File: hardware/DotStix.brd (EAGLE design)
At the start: 20.3 x 50 mm, 20 parts, among them U1 ATMEGA328P-MU-QFN32

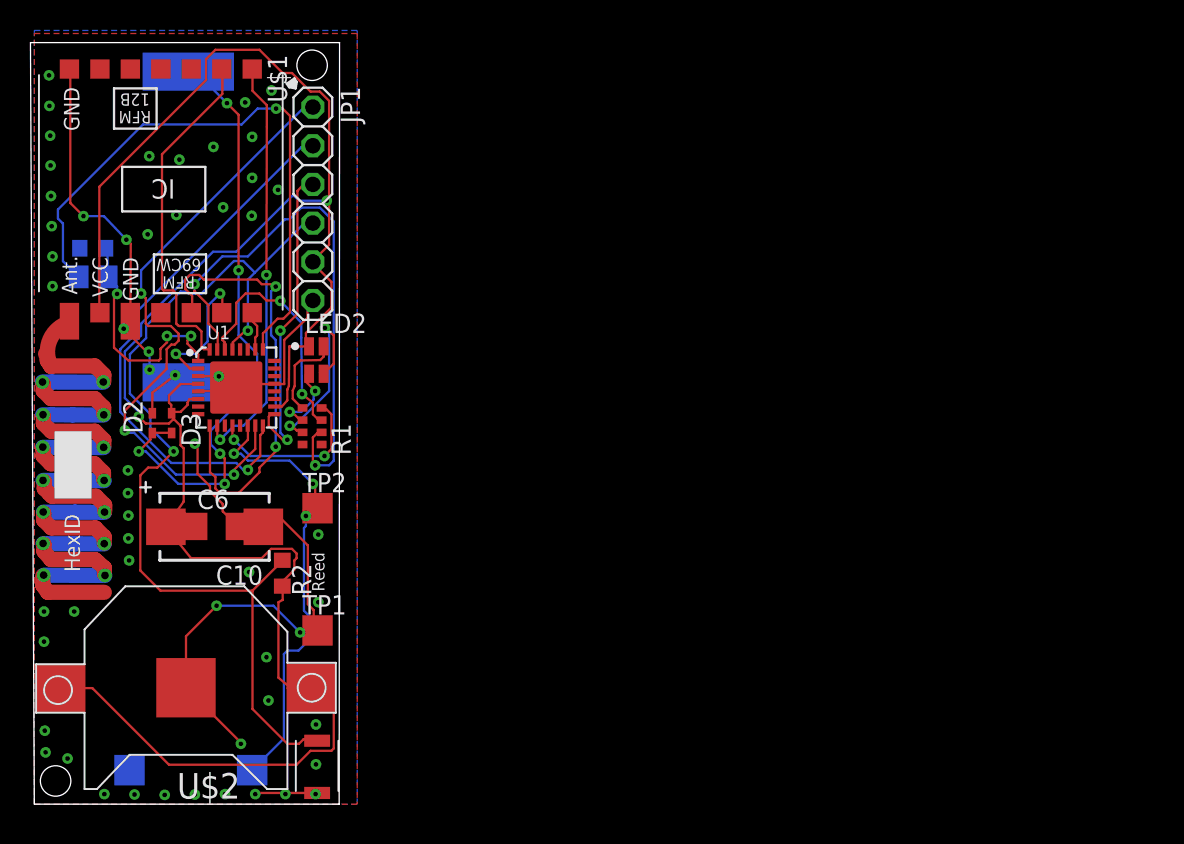
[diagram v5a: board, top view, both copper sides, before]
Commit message: Draft: Fix solar polarity, add 20ppm crystal
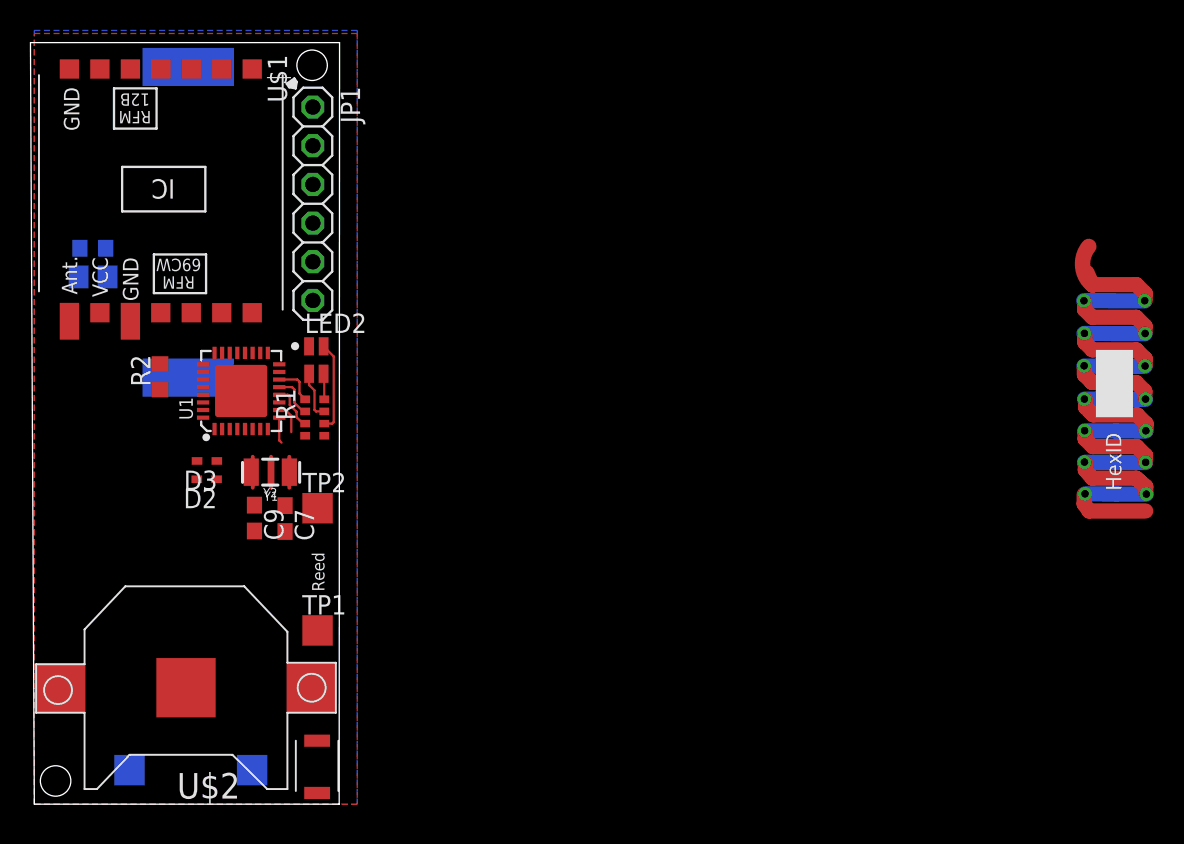
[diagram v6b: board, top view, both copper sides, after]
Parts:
- removed C10: 1500uF 4V, adafruit:CT7343
- removed C6: 100uF 4V, adafruit:C3216
- added C7, C9: 7pF, rcl:C0603
- added Y1: (no value), SparkFun-Clocks:RESONATOR-SMD-3.2X1.3
- added Y2: (no value), SparkFun-Clocks:CRYSTAL-SMD-3.2X1.5MM
- moved R2 15.2 mm to (8.25, 28.1), turned to 90 degrees
- moved D2 5.13 mm to (11.4, 21.3), turned to 180 degrees
- moved D3 3.47 mm to (11.4, 22.5), turned to 180 degrees
- moved R1 0.60 mm to (18.4, 25.4), turned to 270 degrees
- moved U1 0.39 mm to (13.6, 27.1), turned to 90 degrees
- moved D1 0.31 mm to (10.1, 38.2), turned to 270 degrees
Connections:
- removed net ADCENA: U1.13
- removed net LED: R1.4, U1.12
- removed net N$12: LED2.2, R1.6
- removed net N$5: LED2.3, R1.7
- removed net N$9: LED2.1, R1.5
- removed net RXD: R1.3, U1.30
- removed net TXD: R1.2, U1.31
- new net LED_BLUE: R1.2, U1.13
- new net LED_GREEN: R1.1, U1.14
- new net LED_RED: R1.3, U1.12
- new net N$1: LED2.2, R1.7
- new net N$3: LED2.3, R1.8
- new net N$4: LED2.1, R1.6
- new net XTAL1: C9.1, U1.7, Y1.3, Y2.P$2
- new net XTAL2: C7.1, U1.8, Y1.1, Y2.P$1
- net +3V3: no longer C10.+, C6.1
- net GND: now also C7.2, C9.2, D1.-, Y1.2; no longer C10.-, C6.2, D1.+
- net REED: now also U1.31; no longer U1.14
- net SOLAR_RAW: now also D1.+; no longer D1.-
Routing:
- net +3V3: track 142.1 -> 0.00 mm, vias 2 -> 0
- net GND: track 89.2 -> 0.00 mm, vias 57 -> 0
- net RST: track 63.1 -> 0.00 mm, vias 2 -> 0
- net MOSI: track 41.9 -> 0.00 mm, vias 3 -> 0
- net SOLAR_RAW: track 40.4 -> 0.00 mm, vias 5 -> 0
- net LIGHT_SENSE_ENA: track 39.5 -> 0.00 mm, vias 1 -> 0
- net MISO: track 36.5 -> 0.00 mm, vias 1 -> 0
- net TXD: track 36.2 -> 0.00 mm, vias 2 -> 0
- net REED: track 32.0 -> 0.00 mm, vias 3 -> 0
- net RSDI: track 29.5 -> 1.70 mm, vias 2 -> 0
- net RSDO: track 27.4 -> 2.02 mm, vias 2 -> 0
- net RIRQ: track 22.7 -> 0.00 mm
- net SCK: track 20.8 -> 0.00 mm, vias 2 -> 0
- net RXD: track 15.9 -> 0.00 mm, vias 2 -> 0
- net LIGHT_SENSE: track 15.7 -> 0.00 mm, vias 3 -> 0
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
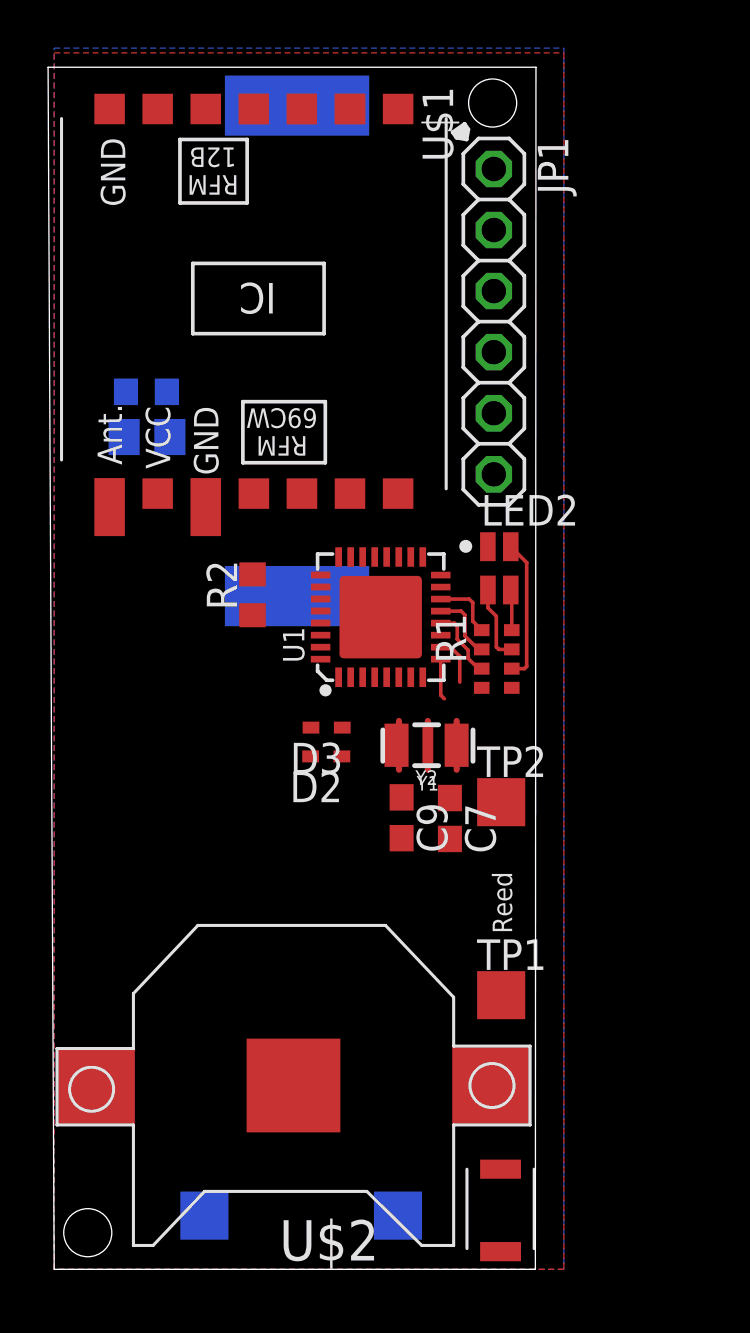
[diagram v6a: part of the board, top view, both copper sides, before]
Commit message: Draft: Fix solar polarity, add 20ppm crystal
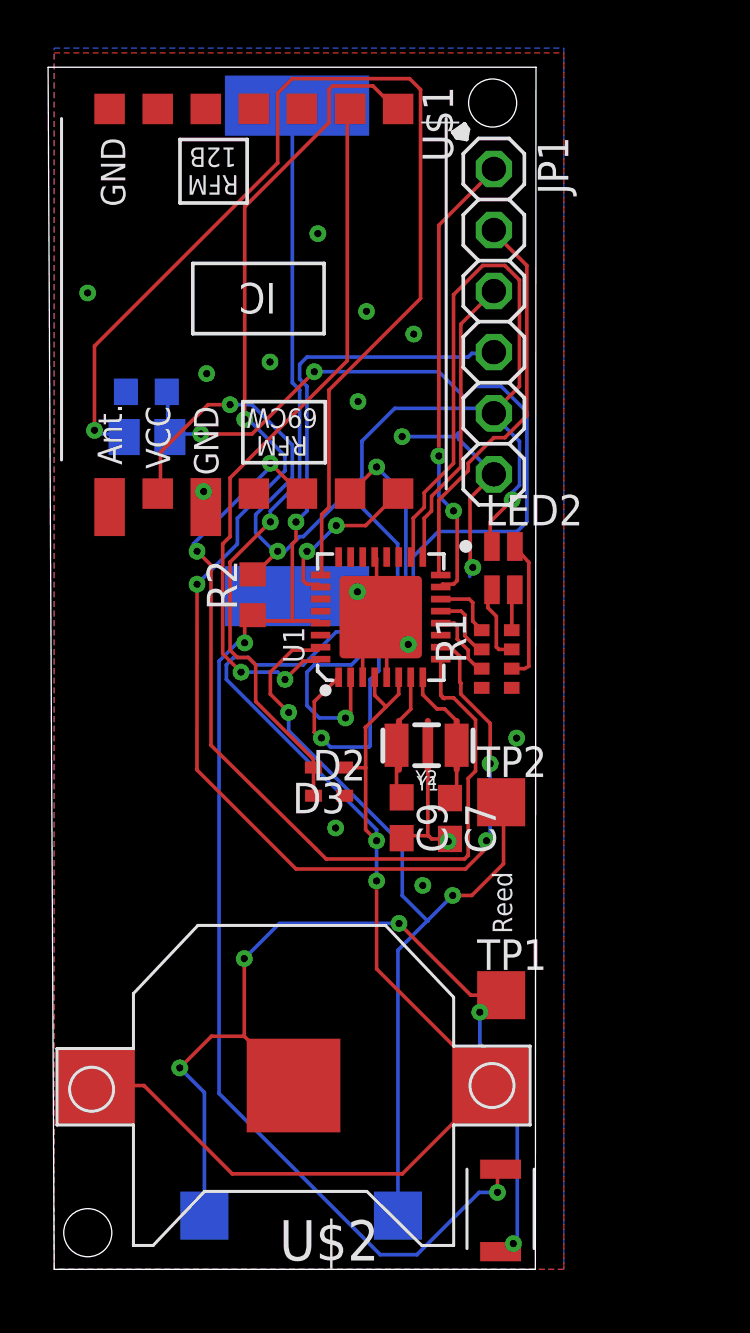
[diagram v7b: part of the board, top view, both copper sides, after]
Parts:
- moved D3 1.66 mm to (11.5, 20.9)
- moved D2 1.64 mm to (11.4, 19.7), turned to 0 degrees
- moved LED2 0.17 mm to (18.7, 29.2)
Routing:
- net +3V3: track 0.00 -> 121.2 mm, vias 0 -> 5
- net GND: track 0.00 -> 70.2 mm, vias 0 -> 21
- net RST: track 0.00 -> 59.4 mm, vias 0 -> 3
- net RSDO: track 2.02 -> 59.0 mm, vias 0 -> 4
- net LIGHT_SENSE_ENA: track 0.00 -> 46.9 mm, vias 0 -> 1
- net LIGHT_SENSE: track 0.00 -> 42.9 mm, vias 0 -> 3
- net RSDI: track 1.70 -> 37.2 mm, vias 0 -> 2
- net REED: track 0.00 -> 35.1 mm, vias 0 -> 2
- net SOLAR_RAW: track 0.00 -> 31.8 mm, vias 0 -> 1
- net RIRQ: track 0.00 -> 29.7 mm, vias 0 -> 2
- net MOSI: track 0.00 -> 19.2 mm, vias 0 -> 2
- net RSCK: track 0.00 -> 18.3 mm, vias 0 -> 2
- net MISO: track 0.00 -> 16.7 mm
- net SCK: track 0.00 -> 12.3 mm
- net RSEL: track 0.00 -> 6.89 mm, vias 0 -> 2
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
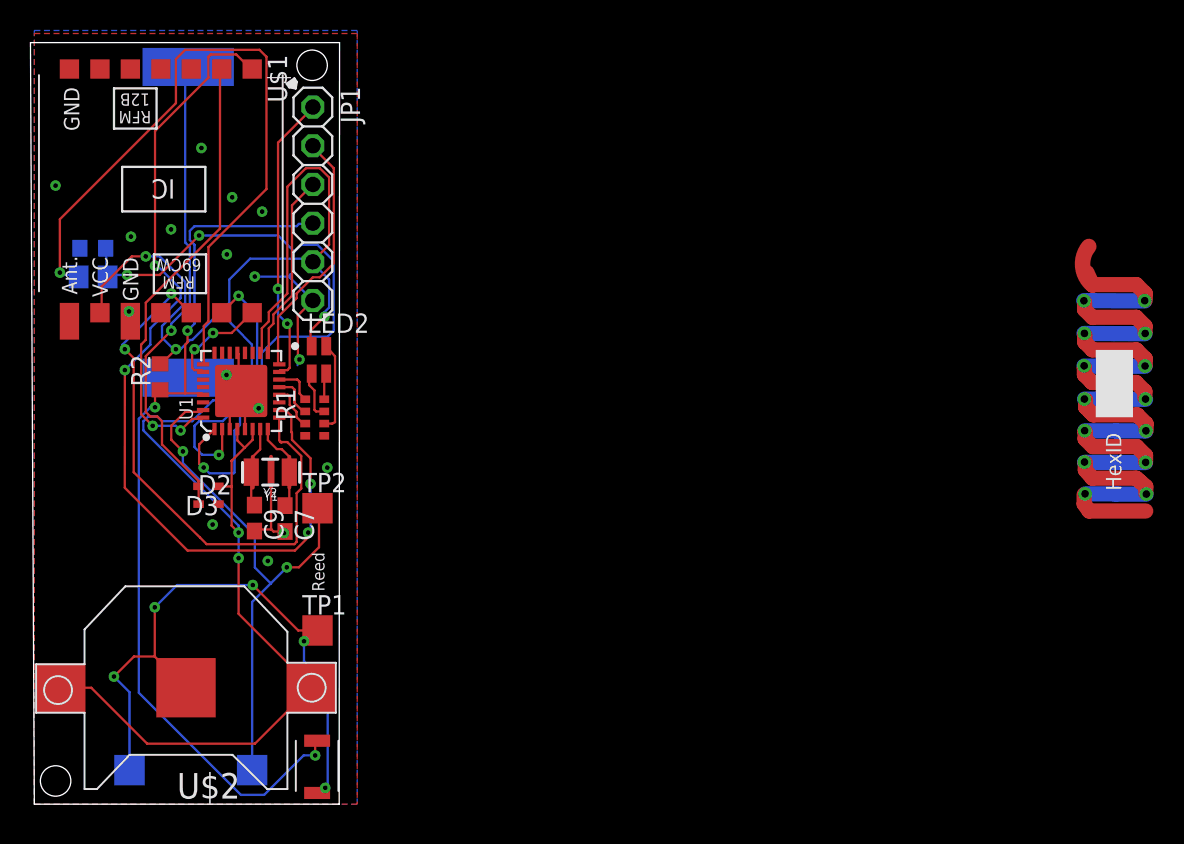
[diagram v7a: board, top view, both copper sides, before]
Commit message: Fix solar polarity, add 20ppm crystal
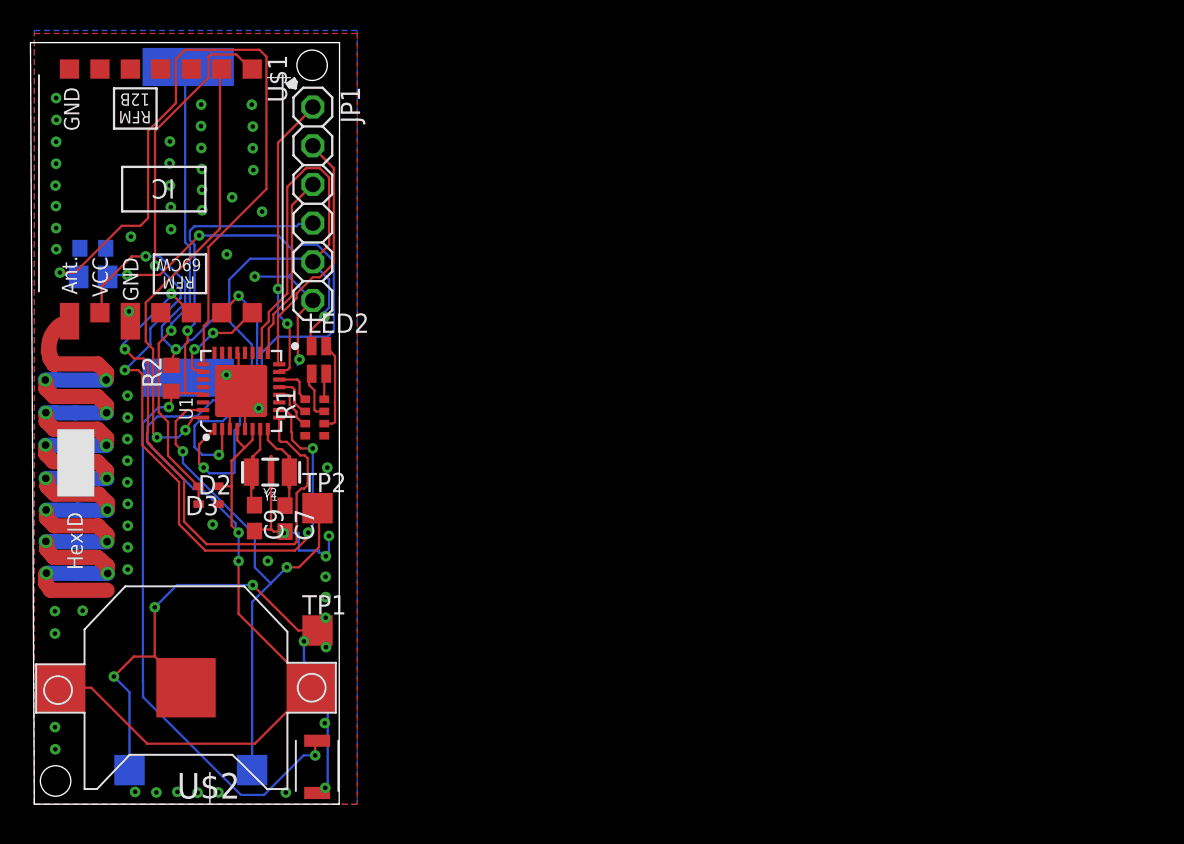
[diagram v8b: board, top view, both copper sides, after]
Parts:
- moved R2 0.74 mm to (8.98, 28.0)
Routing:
- net GND: track 70.2 -> 75.5 mm, vias 21 -> 68
- net LIGHT_SENSE_ENA: track 46.9 -> 48.2 mm
- net SOLAR_RAW: track 31.8 -> 30.8 mm
- net ANT: track 78.2 -> 79.1 mm
- net RSDI: track 37.2 -> 38.0 mm
- net RSDO: track 59.0 -> 59.8 mm
- net RIRQ: track 29.7 -> 30.2 mm
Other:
- board text removed: "Reed"
